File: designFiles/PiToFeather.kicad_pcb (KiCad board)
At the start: 2 copper layers, 3 parts, among them U1 piHeader, U2 featherHeader_12pin, U3 featherHeader_16pin

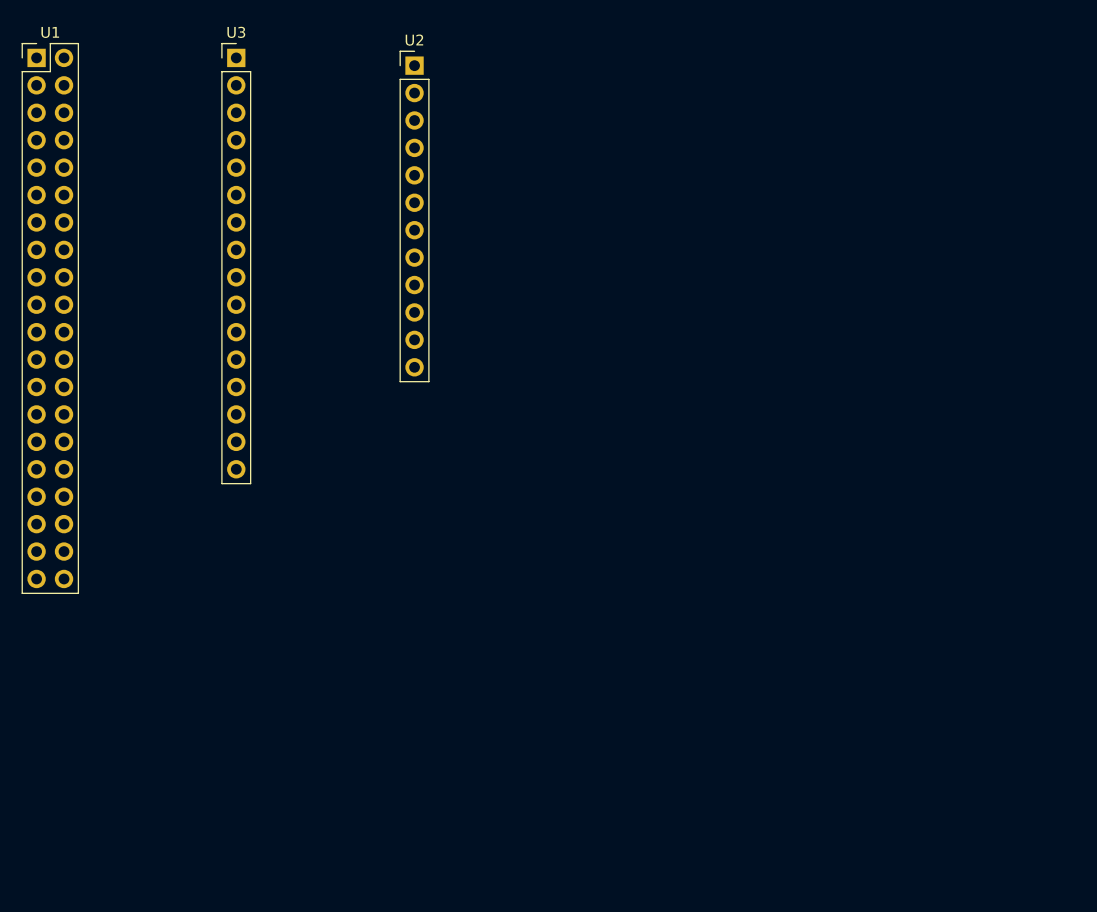
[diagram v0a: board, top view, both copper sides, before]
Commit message: Start layout incl. board outline
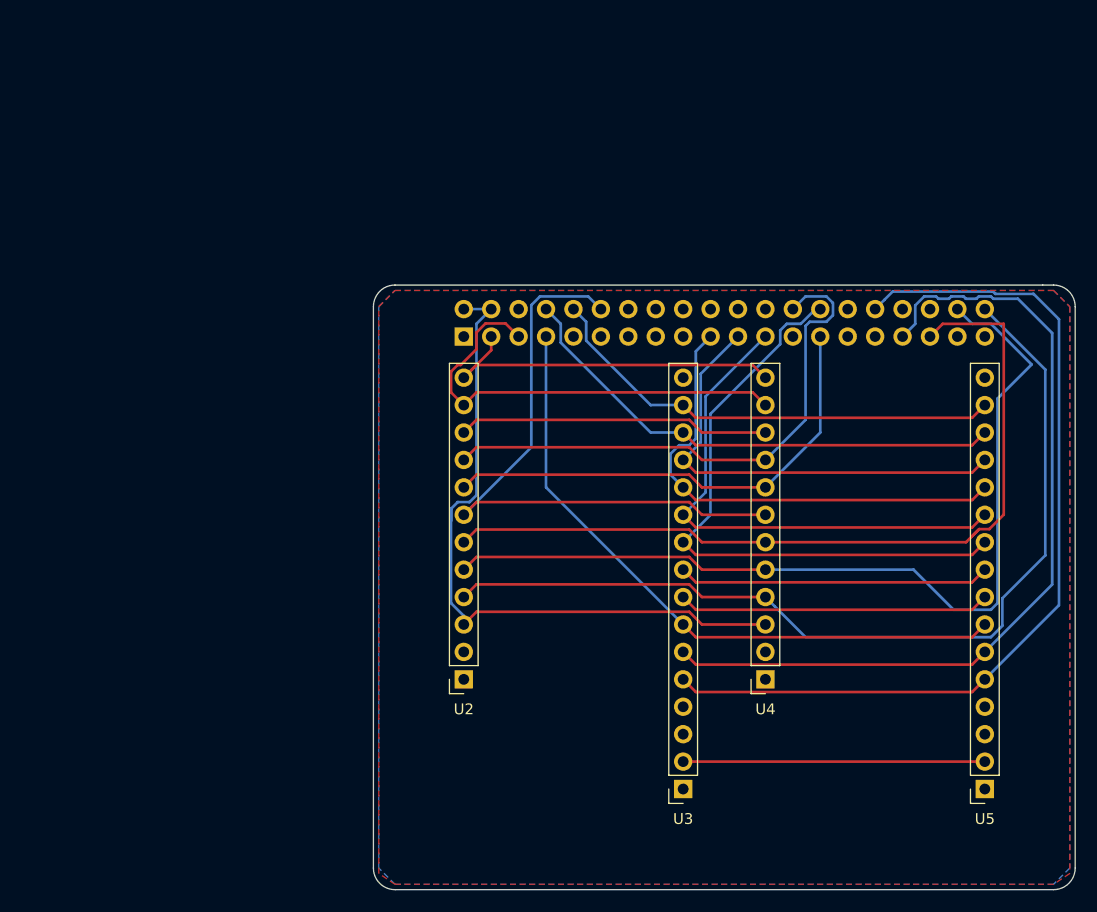
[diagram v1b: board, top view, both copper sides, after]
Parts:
- added U4: featherHeader_12pin, Connector_PinSocket_2.54mm:PinSocket_1x12_P2.54mm_Vertical, F.Cu at (130.3, 112.7)
- added U5: featherHeader_16pin, Connector_PinSocket_2.54mm:PinSocket_1x16_P2.54mm_Vertical, F.Cu at (150.6, 122.9)
- U1: footprint Connector_PinHeader_2.54mm:PinHeader_2x20_P2.54mm_Vertical -> Connector_PinSocket_2.54mm:PinSocket_2x20_P2.54mm_Vertical; moved to B.Cu
- U2: footprint Connector_PinHeader_2.54mm:PinHeader_1x12_P2.54mm_Vertical -> Connector_PinSocket_2.54mm:PinSocket_1x12_P2.54mm_Vertical
- U3: footprint Connector_PinHeader_2.54mm:PinHeader_1x16_P2.54mm_Vertical -> Connector_PinSocket_2.54mm:PinSocket_1x16_P2.54mm_Vertical
- moved U3 79.4 mm to (122.7, 122.9), turned to 180 degrees
- moved U2 57.0 mm to (102.3, 112.7), turned to 180 degrees
- moved U1 47.2 mm to (102.3, 81.0), turned to 270 degrees
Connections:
- U1 pad 11: Net-(U1-Pad11) -> (no net)
- U1 pad 13: Net-(U1-Pad13) -> (no net)
- U1 pad 15: Net-(U1-Pad15) -> (no net)
- U1 pad 16: Net-(U1-Pad16) -> (no net)
- U1 pad 18: Net-(U1-Pad18) -> (no net)
- U1 pad 22: Net-(U1-Pad22) -> (no net)
- U1 pad 36: Net-(U1-Pad36) -> (no net)
- U1 pad 37: Net-(U1-Pad37) -> (no net)
- U2 pad 1: Net-(U2-Pad1) -> (no net)
- U2 pad 2: Net-(U2-Pad2) -> (no net)
- U3 pad 1: Net-(U3-Pad1) -> (no net)
- U3 pad 3: Net-(U3-Pad3) -> (no net)
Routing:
- net PCM_DOUT: track 0.00 -> 86.1 mm
- net PCM_DIN: track 0.00 -> 84.6 mm
- net PWM0: track 0.00 -> 83.9 mm
- net PWM1: track 0.00 -> 79.2 mm
- net PCM_FS: track 0.00 -> 78.1 mm
- net +5V: track 0.00 -> 64.5 mm
- net CLK0: track 0.00 -> 60.8 mm
- net PCM_CLK: track 0.00 -> 58.2 mm
- net ID_SC: track 0.00 -> 56.8 mm
- net CE1: track 0.00 -> 51.4 mm
- net SCK: track 0.00 -> 48.6 mm
- net TX: track 0.00 -> 47.4 mm
- net MOSI: track 0.00 -> 45.5 mm
- net ID_SD: track 0.00 -> 45.0 mm
- net RX: track 0.00 -> 43.8 mm
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- added copper zone on B.Cu, net +3V3
- added copper zone on F.Cu, net GND
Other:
- board outline added: 65 x 56 mm

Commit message: Refinements in routing
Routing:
- net CLK1: track 28.9 -> 74.4 mm
- net CLK2: track 28.9 -> 64.2 mm
- net +3V3: track 27.9 -> 0.00 mm
- net PCM_DIN: track 84.6 -> 60.5 mm
- net PCM_DOUT: track 86.1 -> 64.1 mm
- net CE0: track 28.9 -> 43.3 mm
- net CE1: track 51.4 -> 45.1 mm
- net PWM0: track 83.9 -> 79.1 mm
- net PCM_FS: track 78.1 -> 73.3 mm
- net PWM1: track 79.2 -> 75.9 mm
- net PCM_CLK: track 58.2 -> 60.1 mm
- net SCL: track 42.0 -> 43.9 mm
- net +5V: track 64.5 -> 63.1 mm
- net SDA: track 33.8 -> 35.1 mm
- net MISO: track 42.4 -> 43.3 mm
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
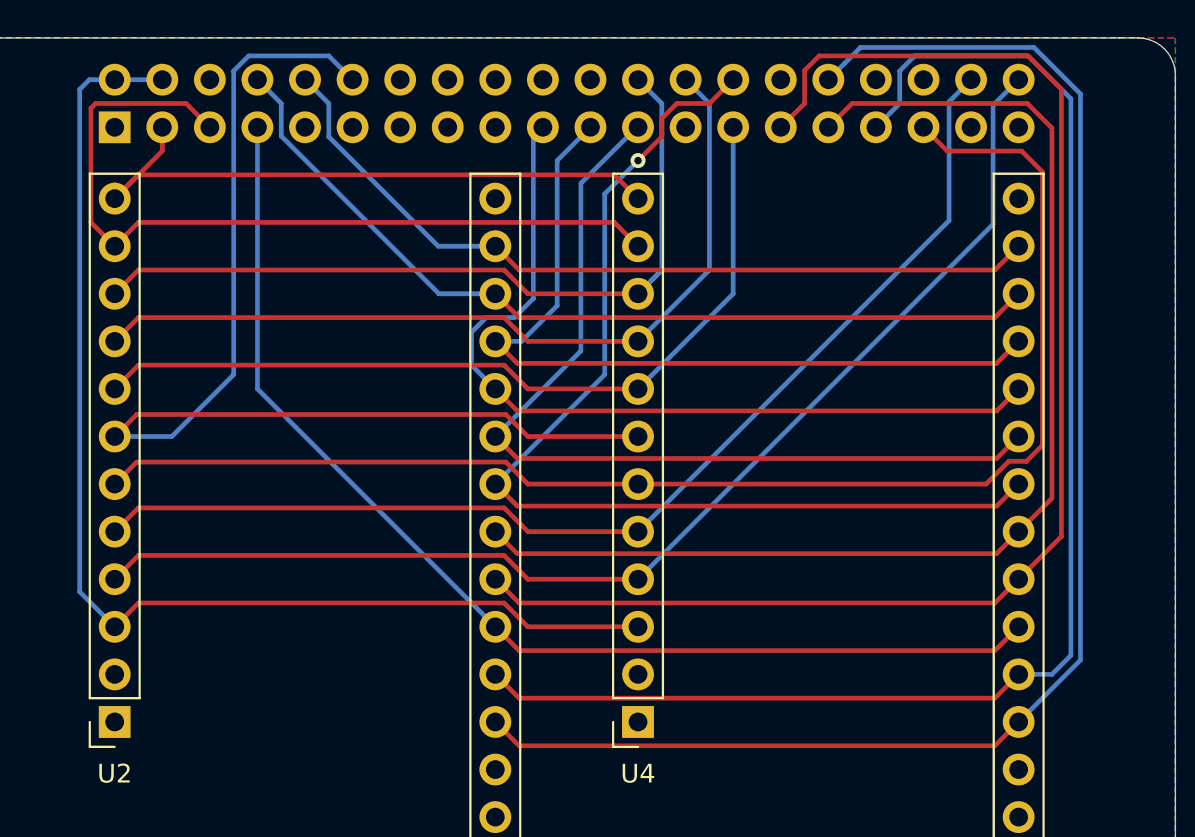
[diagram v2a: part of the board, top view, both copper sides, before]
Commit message: minor improvemnts in routing
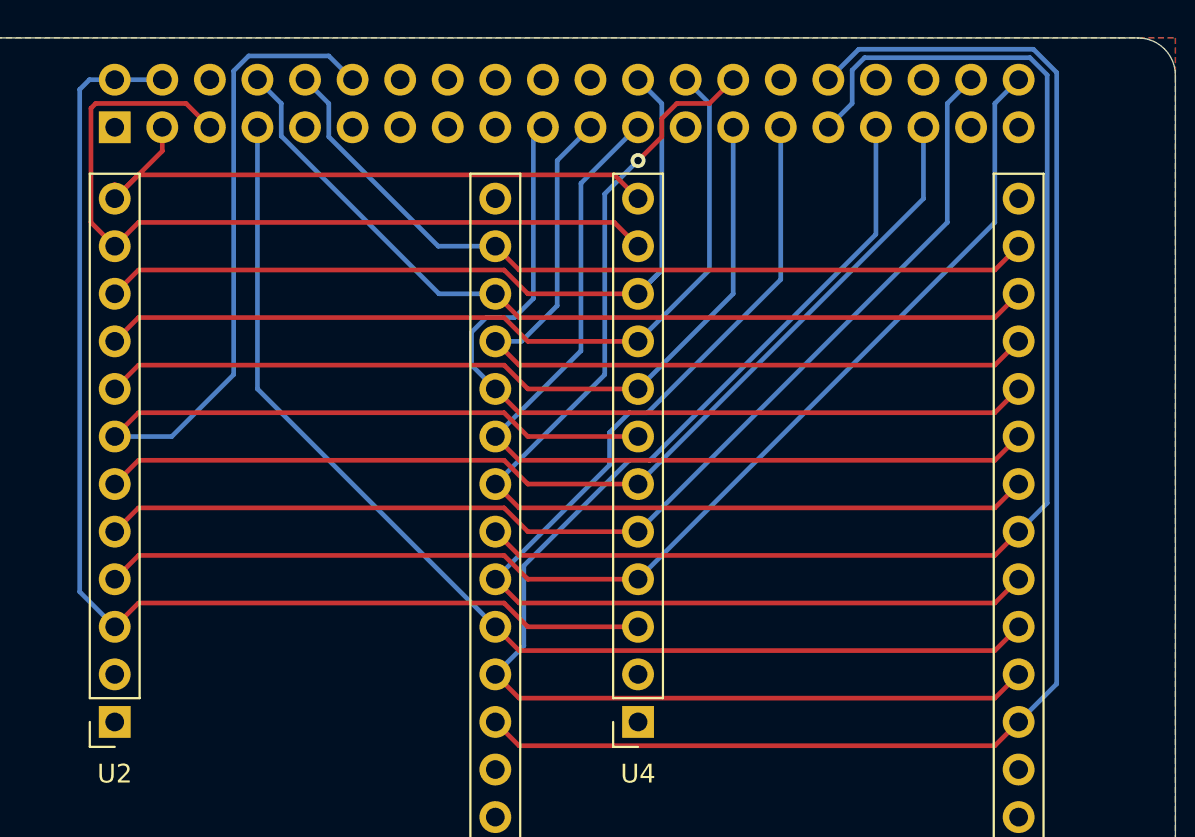
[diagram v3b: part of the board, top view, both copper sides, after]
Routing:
- net PCM_FS: track 73.3 -> 54.4 mm
- net CLK1: track 74.4 -> 60.0 mm
- net PWM1: track 75.9 -> 67.3 mm
- net CLK2: track 64.2 -> 68.7 mm
- net PWM0: track 79.1 -> 77.9 mm

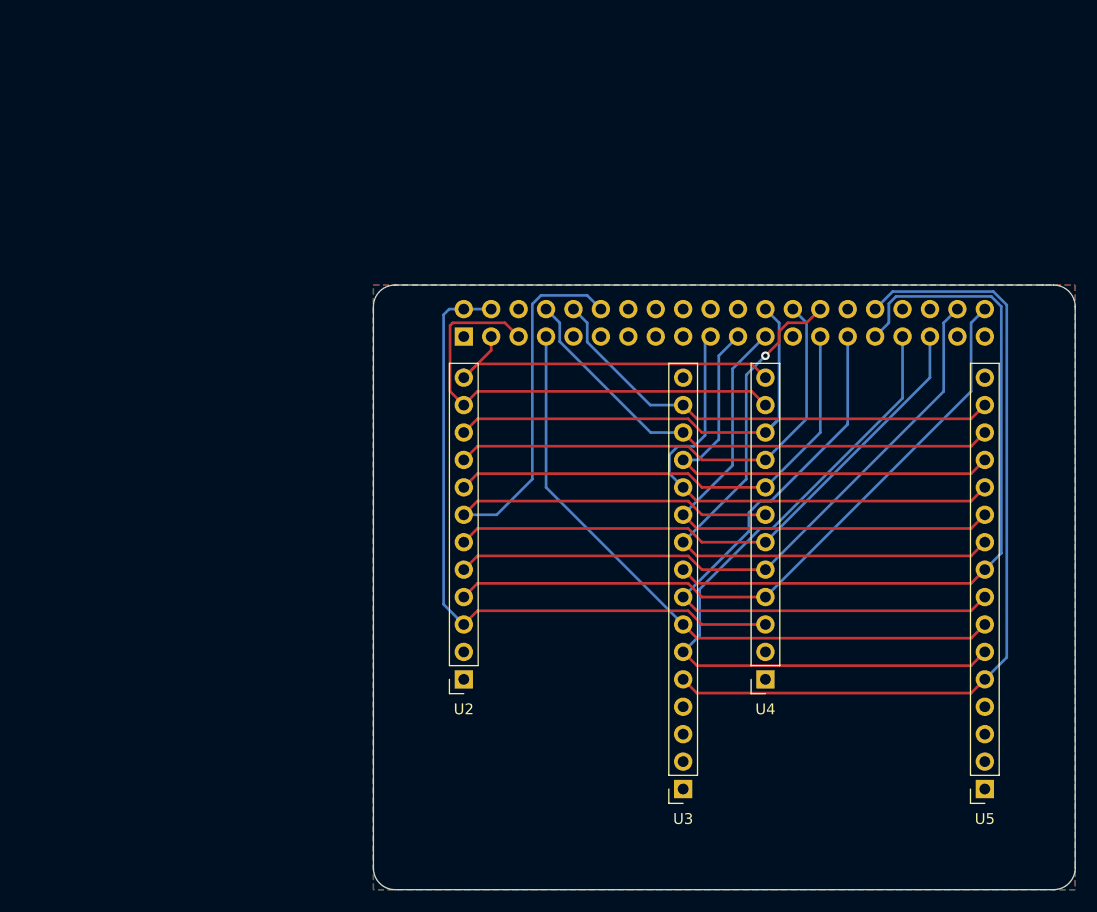
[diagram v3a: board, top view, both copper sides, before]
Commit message: stitching vias added
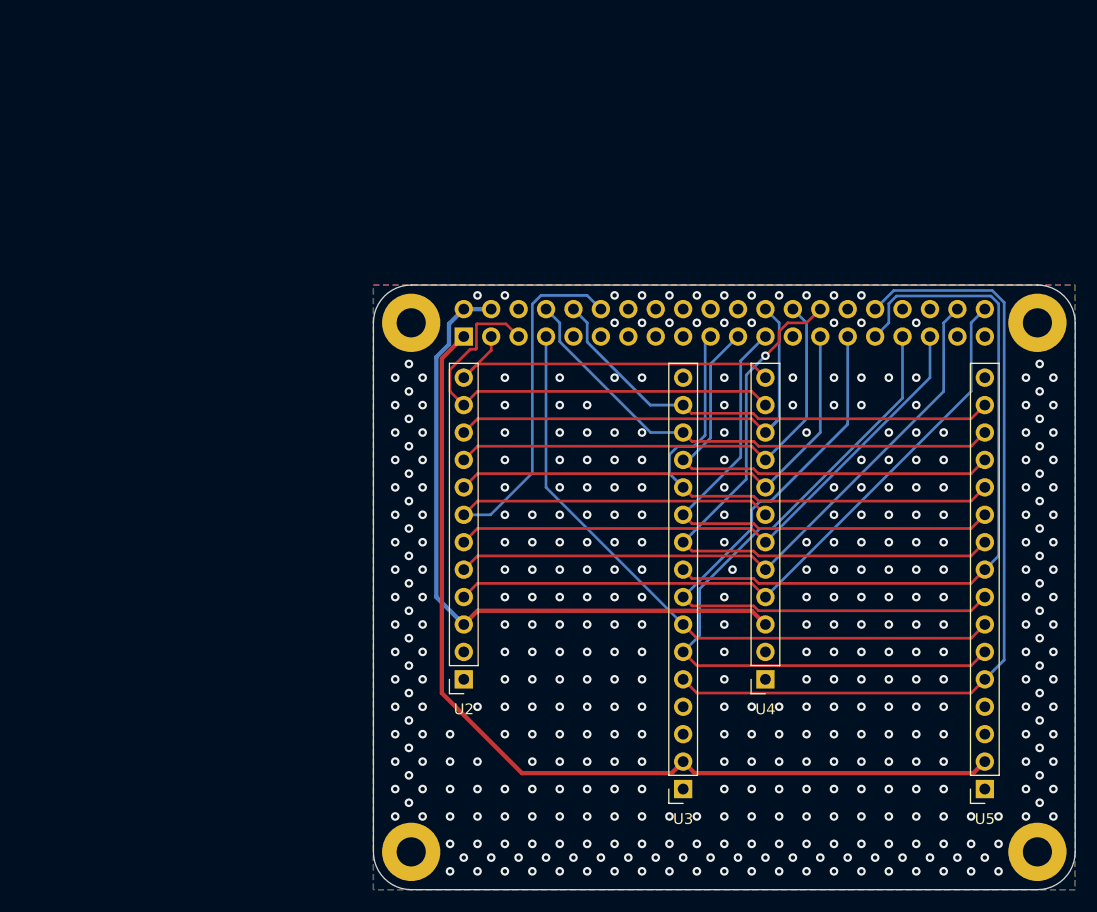
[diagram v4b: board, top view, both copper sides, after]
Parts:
- added H1: MountingHole_Pad, MountingHole:MountingHole_2.7mm_M2.5_Pad, F.Cu at (97.5, 79.7)
- added H2: MountingHole_Pad, MountingHole:MountingHole_2.7mm_M2.5_Pad, F.Cu at (155.5, 79.7)
- added H3: MountingHole_Pad, MountingHole:MountingHole_2.7mm_M2.5_Pad, F.Cu at (155.5, 128.7)
- added H4: MountingHole_Pad, MountingHole:MountingHole_2.7mm_M2.5_Pad, F.Cu at (97.5, 128.7)
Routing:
- net +3V3: track 0.00 -> 88.6 mm
- net SCL: track 43.9 -> 42.7 mm
- net MISO: track 43.3 -> 42.8 mm
- net GND: vias 0 -> 410
- added copper zone on B.Cu, net GND
- removed copper zone on B.Cu, net +3V3
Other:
- outline, holes or cut-outs redrawn
- net class Power added: clearance 0.2, trace_width 0.4, via_dia 0.8, via_drill 0.4
